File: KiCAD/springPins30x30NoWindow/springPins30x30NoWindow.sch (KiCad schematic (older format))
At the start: 21 parts, among them J1 CONN_02X06, J2 CONN_02X06

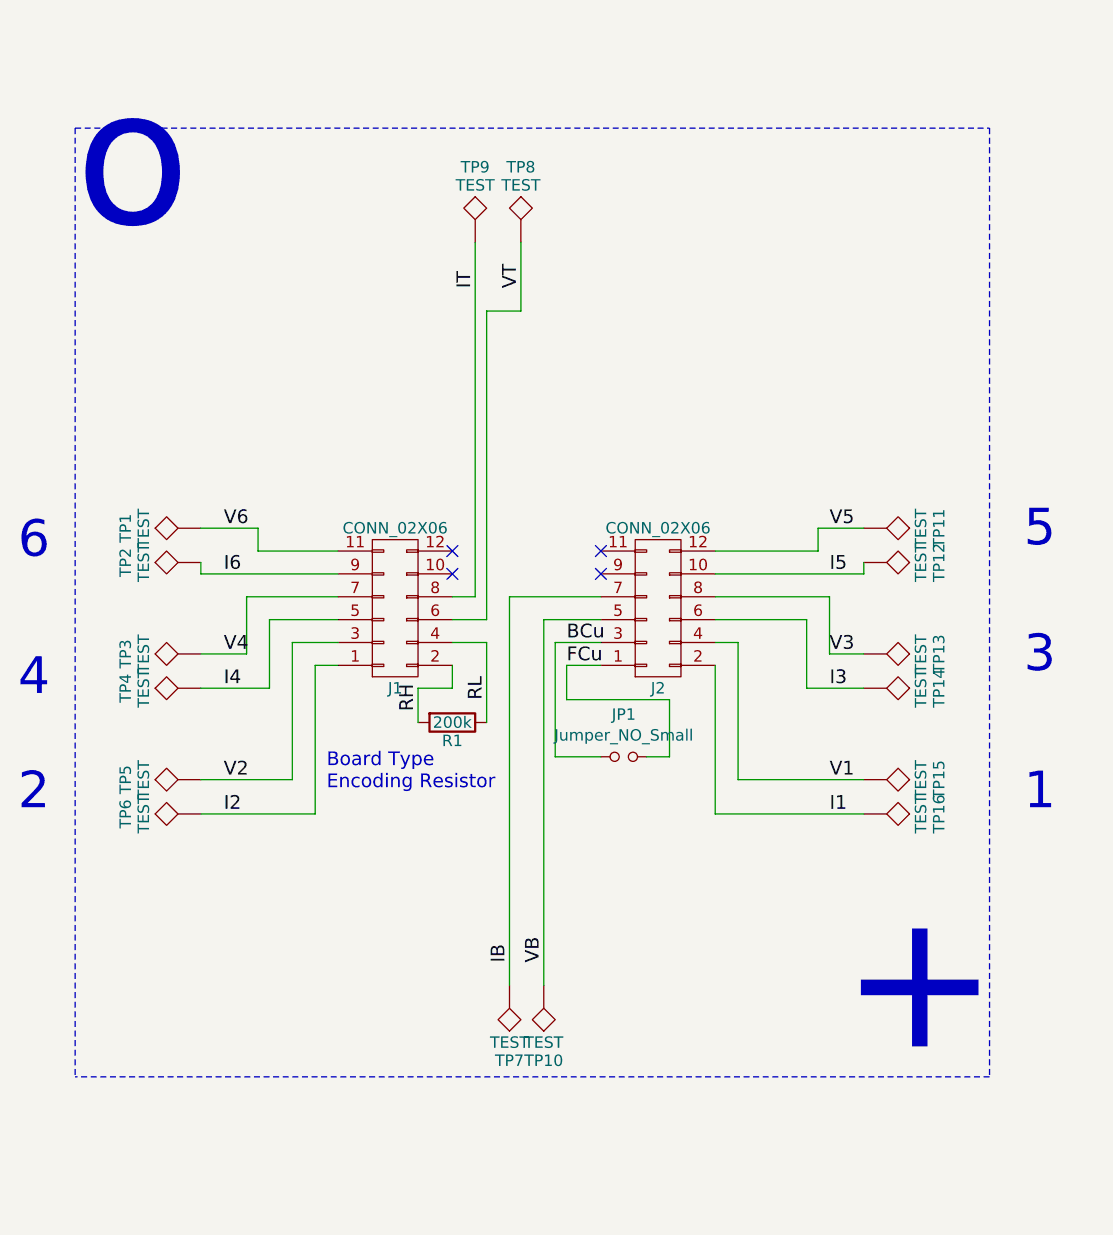
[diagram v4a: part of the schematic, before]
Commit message: go back to old 30x30 springpins layout
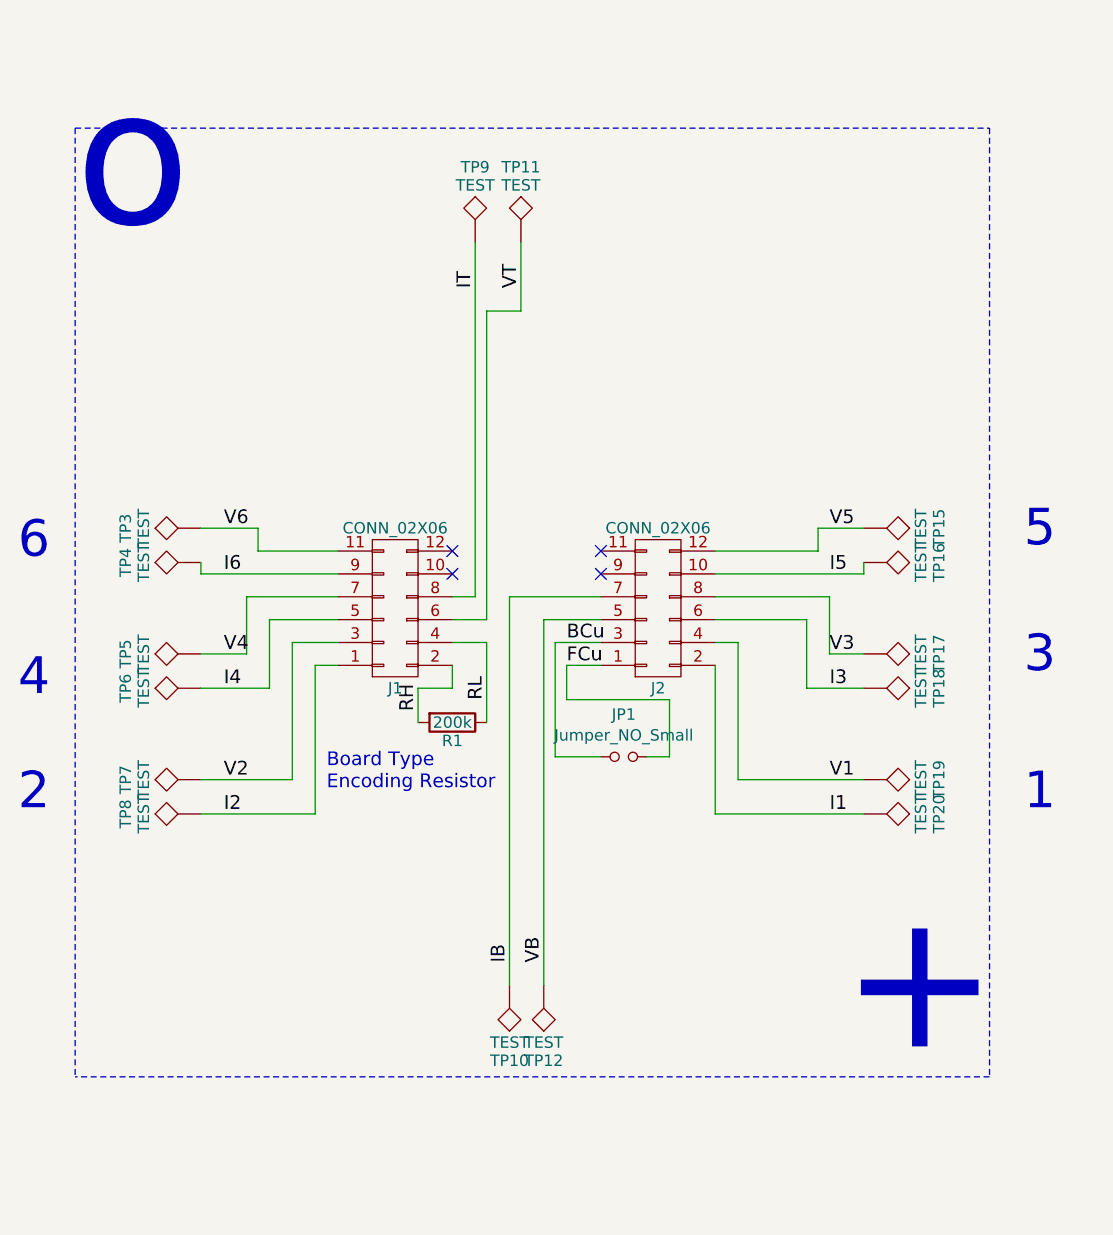
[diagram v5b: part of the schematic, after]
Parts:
- removed TP1, TP13, TP14, TP2: TEST, myParts:S25-022+P25-4023, symbol TEST
- added TP17, TP18, TP19, TP20: TEST, myParts:S25-022+P25-4023, symbol TEST
- TP10, TP11, TP12, TP15, TP16, TP3, TP4, TP5, TP6, TP7, TP8, TP9: farnellCode 9960260 + 9960244 -> (none)
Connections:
- net I1: now also TP20.1; no longer TP16.1
- net I2: now also TP8.1; no longer TP6.1
- net I3: now also TP18.1
- net I4: now also TP6.1; no longer TP4.1
- net I5: now also TP16.1; no longer TP12.1
- net I6: now also TP4.1
- net IB: now also TP10.1; no longer TP7.1
- net V1: now also TP19.1; no longer TP15.1
- net V2: now also TP7.1; no longer TP5.1
- net V3: now also TP17.1
- net V4: now also TP5.1; no longer TP3.1
- net V5: now also TP15.1; no longer TP11.1
- net V6: now also TP3.1
- net VB: now also TP12.1; no longer TP10.1
- net VT: now also TP11.1; no longer TP8.1
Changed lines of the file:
@@
 LIBS:power
 LIBS:device
+LIBS:transistors
+LIBS:conn
 LIBS:linear
 LIBS:regul
+LIBS:74xx
+LIBS:cmos4000
 LIBS:adc-dac
 LIBS:memory
@@
 LIBS:digital-audio
 LIBS:philips
+LIBS:display
 LIBS:cypress
 LIBS:siliconi
@@
 LIBS:atmel
 LIBS:contrib
+LIBS:valves
 LIBS:springPins30x30NoWindow-cache
 EELAYER 26 0
@@
 $EndDescr
 $Comp
+L TEST TP10
+U 1 1 58E4C4C8
+P 5100 5550
+F 0 "TP10" H 5100 5850 50  0000 C BNN
+F 1 "TEST" H 5100 5800 50  0000 C CNN
+F 2 "myParts:S25-022+P25-4023" H 5100 5550 50  0001 C CNN
+F 3 "" H 5100 5550 50  0000 C CNN
+	1    5100 5550
+	-1   0    0    1
+$EndComp
+$Comp
+L TEST TP6
+U 1 1 58E4C4F2
+P 3750 4250
+F 0 "TP6" H 3750 4550 50  0000 C BNN
+F 1 "TEST" H 3750 4500 50  0000 C CNN
+F 2 "myParts:S25-022+P25-4023" H 3750 4250 50  0001 C CNN
+F 3 "" H 3750 4250 50  0000 C CNN
+	1    3750 4250
+	0    -1   -1   0
+$EndComp
+$Comp
+L TEST TP5
+U 1 1 58E4C553
+P 3750 4100
+F 0 "TP5" H 3750 4400 50  0000 C BNN
+F 1 "TEST" H 3750 4350 50  0000 C CNN
+F 2 "myParts:S25-022+P25-4023" H 3750 4100 50  0001 C CNN
+F 3 "" H 3750 4100 50  0000 C CNN
+	1    3750 4100
+	0    -1   -1   0
+$EndComp
+$Comp
+L TEST TP8
+U 1 1 58E4C6B7
+P 3750 4800
+F 0 "TP8" H 3750 5100 50  0000 C BNN
+F 1 "TEST" H 3750 5050 50  0000 C CNN
+F 2 "myParts:S25-022+P25-4023" H 3750 4800 50  0001 C CNN
+F 3 "" H 3750 4800 50  0000 C CNN
+	1    3750 4800
+	0    -1   -1   0
+$EndComp
+$Comp
+L TEST TP7
+U 1 1 58E4C6BD
+P 3750 4650
+F 0 "TP7" H 3750 4950 50  0000 C BNN
+F 1 "TEST" H 3750 4900 50  0000 C CNN
+F 2 "myParts:S25-022+P25-4023" H 3750 4650 50  0001 C CNN
+F 3 "" H 3750 4650 50  0000 C CNN
+	1    3750 4650
+	0    -1   -1   0
+$EndComp
+$Comp
+L TEST TP4
+U 1 1 58E4C747
+P 3750 3700
+F 0 "TP4" H 3750 4000 50  0000 C BNN
+F 1 "TEST" H 3750 3950 50  0000 C CNN
+F 2 "myParts:S25-022+P25-4023" H 3750 3700 50  0001 C CNN
+F 3 "" H 3750 3700 50  0000 C CNN
+	1    3750 3700
+	0    -1   -1   0
+$EndComp
+$Comp
+L TEST TP3
+U 1 1 58E4C74D
+P 3750 3550
+F 0 "TP3" H 3750 3850 50  0000 C BNN
+F 1 "TEST" H 3750 3800 50  0000 C CNN
+F 2 "myParts:S25-022+P25-4023" H 3750 3550 50  0001 C CNN
+F 3 "" H 3750 3550 50  0000 C CNN
+	1    3750 3550
+	0    -1   -1   0
+$EndComp
+$Comp
+L TEST TP18
+U 1 1 58E4CA5F
+P 6650 4250
+F 0 "TP18" H 6650 4550 50  0000 C BNN
+F 1 "TEST" H 6650 4500 50  0000 C CNN
+F 2 "myParts:S25-022+P25-4023" H 6650 4250 50  0001 C CNN
+F 3 "" H 6650 4250 50  0000 C CNN
+	1    6650 4250
+	0    1    -1   0
+$EndComp
+$Comp
+L TEST TP17
+U 1 1 58E4CA65
+P 6650 4100
+F 0 "TP17" H 6650 4400 50  0000 C BNN
+F 1 "TEST" H 6650 4350 50  0000 C CNN
+F 2 "myParts:S25-022+P25-4023" H 6650 4100 50  0001 C CNN
+F 3 "" H 6650 4100 50  0000 C CNN
+	1    6650 4100
+	0    1    -1   0
+$EndComp
+$Comp
+L TEST TP20
+U 1 1 58E4CA6B
+P 6650 4800
+F 0 "TP20" H 6650 5100 50  0000 C BNN
+F 1 "TEST" H 6650 5050 50  0000 C CNN
+F 2 "myParts:S25-022+P25-4023" H 6650 4800 50  0001 C CNN
+F 3 "" H 6650 4800 50  0000 C CNN
+	1    6650 4800
+	0    1    -1   0
+$EndComp
+$Comp
+L TEST TP19
+U 1 1 58E4CA71
+P 6650 4650
+F 0 "TP19" H 6650 4950 50  0000 C BNN
+F 1 "TEST" H 6650 4900 50  0000 C CNN
+F 2 "myParts:S25-022+P25-4023" H 6650 4650 50  0001 C CNN
+F 3 "" H 6650 4650 50  0000 C CNN
+	1    6650 4650
+	0    1    -1   0
+$EndComp
+$Comp
+L TEST TP16
+U 1 1 58E4CA77
+P 6650 3700
+F 0 "TP16" H 6650 4000 50  0000 C BNN
+F 1 "TEST" H 6650 3950 50  0000 C CNN
+F 2 "myParts:S25-022+P25-4023" H 6650 3700 50  0001 C CNN
+F 3 "" H 6650 3700 50  0000 C CNN
+	1    6650 3700
+	0    1    -1   0
+$EndComp
+$Comp
+L TEST TP15
+U 1 1 58E4CA7D
+P 6650 3550
+F 0 "TP15" H 6650 3850 50  0000 C BNN
+F 1 "TEST" H 6650 3800 50  0000 C CNN
+F 2 "myParts:S25-022+P25-4023" H 6650 3550 50  0001 C CNN
+F 3 "" H 6650 3550 50  0000 C CNN
+	1    6650 3550
+	0    1    -1   0
+$EndComp
+$Comp
 L TEST TP9
 U 1 1 58E4CC43
@@
 F 2 "myParts:S25-022+P25-4023" H 4950 2300 50  0001 C CNN
 F 3 "" H 4950 2300 50  0000 C CNN
-F 4 "9960260 + 9960244" H 4950 2300 60  0001 C CNN "farnellCode"
 	1    4950 2300
+	-1   0    0    -1
+$EndComp
+$Comp
+L TEST TP11
+U 1 1 58E4CC49
+P 5150 2300
+F 0 "TP11" H 5150 2600 50  0000 C BNN
+F 1 "TEST" H 5150 2550 50  0000 C CNN
+F 2 "myParts:S25-022+P25-4023" H 5150 2300 50  0001 C CNN
+F 3 "" H 5150 2300 50  0000 C CNN
+	1    5150 2300
 	-1   0    0    -1
 $EndComp
@@
 Wire Wire Line
 	4000 3550 3750 3550
+$Comp
+L TEST TP12
+U 1 1 58E4C3ED
+P 5250 5550
+F 0 "TP12" H 5250 5850 50  0000 C BNN
+F 1 "TEST" H 5250 5800 50  0000 C CNN
+F 2 "myParts:S25-022+P25-4023" H 5250 5550 50  0001 C CNN
+F 3 "" H 5250 5550 50  0000 C CNN
+	1    5250 5550
+	-1   0    0    1
+$EndComp
 Wire Wire Line
 	4950 2300 4950 3850
@@
 Wire Wire Line
 	5800 4550 5700 4550
-$Comp
-L TEST TP8
-U 1 1 5A65C96D
-P 5150 2300
-F 0 "TP8" H 5150 2600 50  0000 C BNN
-F 1 "TEST" H 5150 2550 50  0000 C CNN
-F 2 "myParts:S25-022+P25-4023" H 5150 2300 50  0001 C CNN
-F 3 "" H 5150 2300 50  0000 C CNN
-F 4 "9960260 + 9960244" H 5150 2300 60  0001 C CNN "farnellCode"
-	1    5150 2300
-	-1   0    0    -1
-$EndComp
-$Comp
-L TEST TP11
-U 1 1 5A65C9A7
-P 6650 3550
-F 0 "TP11" H 6650 3850 50  0000 C BNN
-F 1 "TEST" H 6650 3800 50  0000 C CNN
-F 2 "myParts:S25-022+P25-4023" H 6650 3550 50  0001 C CNN
-F 3 "" H 6650 3550 50  0000 C CNN
-F 4 "9960260 + 9960244" H 6650 3550 60  0001 C CNN "farnellCode"
-	1    6650 3550
-	0    1    -1   0
-$EndComp
-$Comp
-L TEST TP12
-U 1 1 5A65CA0A
-P 6650 3700
-F 0 "TP12" H 6650 4000 50  0000 C BNN
-F 1 "TEST" H 6650 3950 50  0000 C CNN
-F 2 "myParts:S25-022+P25-4023" H 6650 3700 50  0001 C CNN
-F 3 "" H 6650 3700 50  0000 C CNN
-F 4 "9960260 + 9960244" H 6650 3700 60  0001 C CNN "farnellCode"
-	1    6650 3700
-	0    1    -1   0
-$EndComp
-$Comp
-L TEST TP13
-U 1 1 5A65CA32
-P 6650 4100
-F 0 "TP13" H 6650 4400 50  0000 C BNN
-F 1 "TEST" H 6650 4350 50  0000 C CNN
-F 2 "myParts:S25-022+P25-4023" H 6650 4100 50  0001 C CNN
-F 3 "" H 6650 4100 50  0000 C CNN
-F 4 "9960260 + 9960244" H 6650 4100 60  0001 C CNN "farnellCode"
-	1    6650 4100
-	0    1    -1   0
-$EndComp
-$Comp
-L TEST TP14
-U 1 1 5A65CA62
-P 6650 4250
-F 0 "TP14" H 6650 4550 50  0000 C BNN
-F 1 "TEST" H 6650 4500 50  0000 C CNN
-F 2 "myParts:S25-022+P25-4023" H 6650 4250 50  0001 C CNN
-F 3 "" H 6650 4250 50  0000 C CNN
-F 4 "9960260 + 9960244" H 6650 4250 60  0001 C CNN "farnellCode"
-	1    6650 4250
-	0    1    -1   0
-$EndComp
-$Comp
-L TEST TP15
-U 1 1 5A65CA8E
-P 6650 4650
-F 0 "TP15" H 6650 4950 50  0000 C BNN
-F 1 "TEST" H 6650 4900 50  0000 C CNN
-F 2 "myParts:S25-022+P25-4023" H 6650 4650 50  0001 C CNN
-F 3 "" H 6650 4650 50  0000 C CNN
-F 4 "9960260 + 9960244" H 6650 4650 60  0001 C CNN "farnellCode"
-	1    6650 4650
-	0    1    -1   0
-$EndComp
-$Comp
-L TEST TP16
-U 1 1 5A65CAC6
-P 6650 4800
-F 0 "TP16" H 6650 5100 50  0000 C BNN
-F 1 "TEST" H 6650 5050 50  0000 C CNN
-F 2 "myParts:S25-022+P25-4023" H 6650 4800 50  0001 C CNN
-F 3 "" H 6650 4800 50  0000 C CNN
-F 4 "9960260 + 9960244" H 6650 4800 60  0001 C CNN "farnellCode"
-	1    6650 4800
-	0    1    -1   0
-$EndComp
-$Comp
-L TEST TP10
-U 1 1 5A65CAF2
-P 5250 5550
-F 0 "TP10" H 5250 5850 50  0000 C BNN
-F 1 "TEST" H 5250 5800 50  0000 C CNN
-F 2 "myParts:S25-022+P25-4023" H 5250 5550 50  0001 C CNN
-F 3 "" H 5250 5550 50  0000 C CNN
-F 4 "9960260 + 9960244" H 5250 5550 60  0001 C CNN "farnellCode"
-	1    5250 5550
-	1    0    0    1
-$EndComp
-$Comp
-L TEST TP7
-U 1 1 5A65CB55
-P 5100 5550
-F 0 "TP7" H 5100 5850 50  0000 C BNN
-F 1 "TEST" H 5100 5800 50  0000 C CNN
-F 2 "myParts:S25-022+P25-4023" H 5100 5550 50  0001 C CNN
-F 3 "" H 5100 5550 50  0000 C CNN
-F 4 "9960260 + 9960244" H 5100 5550 60  0001 C CNN "farnellCode"
-	1    5100 5550
-	1    0    0    1
-$EndComp
-$Comp
-L TEST TP6
-U 1 1 5A65CC03
-P 3750 4800
-F 0 "TP6" H 3750 5100 50  0000 C BNN
-F 1 "TEST" H 3750 5050 50  0000 C CNN
-F 2 "myParts:S25-022+P25-4023" H 3750 4800 50  0001 C CNN
-F 3 "" H 3750 4800 50  0000 C CNN
-F 4 "9960260 + 9960244" H 3750 4800 60  0001 C CNN "farnellCode"
-	1    3750 4800
-	0    -1   1    0
-$EndComp
-$Comp
-L TEST TP5
-U 1 1 5A65CC8C
-P 3750 4650
-F 0 "TP5" H 3750 4950 50  0000 C BNN
-F 1 "TEST" H 3750 4900 50  0000 C CNN
-F 2 "myParts:S25-022+P25-4023" H 3750 4650 50  0001 C CNN
-F 3 "" H 3750 4650 50  0000 C CNN
-F 4 "9960260 + 9960244" H 3750 4650 60  0001 C CNN "farnellCode"
-	1    3750 4650
-	0    -1   1    0
-$EndComp
-$Comp
-L TEST TP4
-U 1 1 5A65CCC0
-P 3750 4250
-F 0 "TP4" H 3750 4550 50  0000 C BNN
-F 1 "TEST" H 3750 4500 50  0000 C CNN
-F 2 "myParts:S25-022+P25-4023" H 3750 4250 50  0001 C CNN
-F 3 "" H 3750 4250 50  0000 C CNN
-F 4 "9960260 + 9960244" H 3750 4250 60  0001 C CNN "farnellCode"
-	1    3750 4250
-	0    -1   1    0
-$EndComp
-$Comp
-L TEST TP3
-U 1 1 5A65CCFE
-P 3750 4100
-F 0 "TP3" H 3750 4400 50  0000 C BNN
-F 1 "TEST" H 3750 4350 50  0000 C CNN
-F 2 "myParts:S25-022+P25-4023" H 3750 4100 50  0001 C CNN
-F 3 "" H 3750 4100 50  0000 C CNN
-F 4 "9960260 + 9960244" H 3750 4100 60  0001 C CNN "farnellCode"
-	1    3750 4100
-	0    -1   1    0
-$EndComp
-$Comp
-L TEST TP2
-U 1 1 5A65CD36
-P 3750 3700
-F 0 "TP2" H 3750 4000 50  0000 C BNN
-F 1 "TEST" H 3750 3950 50  0000 C CNN
-F 2 "myParts:S25-022+P25-4023" H 3750 3700 50  0001 C CNN
-F 3 "" H 3750 3700 50  0000 C CNN
-F 4 "9960260 + 9960244" H 3750 3700 60  0001 C CNN "farnellCode"
-	1    3750 3700
-	0    -1   1    0
-$EndComp
-$Comp
-L TEST TP1
-U 1 1 5A65CD7A
-P 3750 3550
-F 0 "TP1" H 3750 3850 50  0000 C BNN
-F 1 "TEST" H 3750 3800 50  0000 C CNN
-F 2 "myParts:S25-022+P25-4023" H 3750 3550 50  0001 C CNN
-F 3 "" H 3750 3550 50  0000 C CNN
-F 4 "9960260 + 9960244" H 3750 3550 60  0001 C CNN "farnellCode"
-	1    3750 3550
-	0    -1   1    0
-$EndComp
 $EndSCHEMATC

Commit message: spruce up spring pin boards
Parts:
- J1, J2: symbol CONN_02X06 -> Connector:Conn_02x06_Odd_Even
- JP1: symbol Jumper_NO_Small -> device:Jumper_NO_Small
- L1: symbol GREY@CHRISTOFORO.NET -> myParts:GREY@CHRISTOFORO.NET
- R1: symbol R -> device:R
- TP10, TP11, TP12, TP15, TP16, TP17, TP18, TP19, TP20, TP3, TP4, TP5, TP6, TP7, TP8, TP9: symbol TEST -> Connector:Test_Point
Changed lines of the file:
@@
-EESchema Schematic File Version 2
-LIBS:myParts
-LIBS:power
-LIBS:device
-LIBS:transistors
-LIBS:conn
-LIBS:linear
-LIBS:regul
-LIBS:74xx
-LIBS:cmos4000
-LIBS:adc-dac
-LIBS:memory
-LIBS:xilinx
-LIBS:microcontrollers
-LIBS:dsp
-LIBS:microchip
-LIBS:analog_switches
-LIBS:motorola
-LIBS:texas
-LIBS:intel
-LIBS:audio
-LIBS:interface
-LIBS:digital-audio
-LIBS:philips
-LIBS:display
-LIBS:cypress
-LIBS:siliconi
-LIBS:opto
-LIBS:atmel
-LIBS:contrib
-LIBS:valves
+EESchema Schematic File Version 4
 LIBS:springPins30x30NoWindow-cache
 EELAYER 26 0
@@
 $EndDescr
 $Comp
-L TEST TP10
+L Connector:Test_Point TP10
 U 1 1 58E4C4C8
 P 5100 5550
@@
 $EndComp
 $Comp
-L TEST TP6
+L Connector:Test_Point TP6
 U 1 1 58E4C4F2
 P 3750 4250
@@
 $EndComp
 $Comp
-L TEST TP5
+L Connector:Test_Point TP5
 U 1 1 58E4C553
 P 3750 4100
@@
 $EndComp
 $Comp
-L TEST TP8
+L Connector:Test_Point TP8
 U 1 1 58E4C6B7
 P 3750 4800
@@
 $EndComp
 $Comp
-L TEST TP7
+L Connector:Test_Point TP7
 U 1 1 58E4C6BD
 P 3750 4650
@@
 $EndComp
 $Comp
-L TEST TP4
+L Connector:Test_Point TP4
 U 1 1 58E4C747
 P 3750 3700
@@
 $EndComp
 $Comp
-L TEST TP3
+L Connector:Test_Point TP3
 U 1 1 58E4C74D
 P 3750 3550
@@
 $EndComp
 $Comp
-L TEST TP18
+L Connector:Test_Point TP18
 U 1 1 58E4CA5F
 P 6650 4250
@@
 $EndComp
 $Comp
-L TEST TP17
+L Connector:Test_Point TP17
 U 1 1 58E4CA65
 P 6650 4100
@@
 $EndComp
 $Comp
-L TEST TP20
+L Connector:Test_Point TP20
 U 1 1 58E4CA6B
 P 6650 4800
@@
 $EndComp
 $Comp
-L TEST TP19
+L Connector:Test_Point TP19
 U 1 1 58E4CA71
 P 6650 4650
@@
 $EndComp
 $Comp
-L TEST TP16
+L Connector:Test_Point TP16
 U 1 1 58E4CA77
 P 6650 3700
@@
 $EndComp
 $Comp
-L TEST TP15
+L Connector:Test_Point TP15
 U 1 1 58E4CA7D
 P 6650 3550
@@
 $EndComp
 $Comp
-L TEST TP9
+L Connector:Test_Point TP9
 U 1 1 58E4CC43
 P 4950 2300
@@
 $EndComp
 $Comp
-L TEST TP11
+L Connector:Test_Point TP11
 U 1 1 58E4CC49
 P 5150 2300
@@
 6
 $Comp
-L CONN_02X06 J1
+L Connector:Conn_02x06_Odd_Even J1
 U 1 1 599DB107
-P 4600 3900
-F 0 "J1" H 4600 4250 50  0000 C CNN
-F 1 "CONN_02X06" H 4600 3550 50  0000 C CNN
-F 2 "Pin_Headers:Pin_Header_Straight_2x06_Pitch2.54mm" H 4600 2700 50  0001 C CNN
-F 3 "" H 4600 2700 50  0001 C CNN
-	1    4600 3900
+P 4550 3950
+F 0 "J1" H 4450 4250 50  0000 C CNN
+F 1 "CONN_02X06" H 4550 3500 50  0000 C CNN
+F 2 "Pin_Headers:Pin_Header_Straight_2x06_Pitch2.54mm" H 4550 2750 50  0001 C CNN
+F 3 "" H 4550 2750 50  0001 C CNN
+	1    4550 3950
 	1    0    0    1
 $EndComp
 $Comp
-L CONN_02X06 J2
+L Connector:Conn_02x06_Odd_Even J2
 U 1 1 599DB1BB
-P 5750 3900
-F 0 "J2" H 5750 4250 50  0000 C CNN
-F 1 "CONN_02X06" H 5750 3550 50  0000 C CNN
-F 2 "Pin_Headers:Pin_Header_Straight_2x06_Pitch2.54mm" H 5750 2700 50  0001 C CNN
-F 3 "" H 5750 2700 50  0001 C CNN
-	1    5750 3900
+P 5700 3950
+F 0 "J2" H 5600 4250 50  0000 C CNN
+F 1 "CONN_02X06" H 5700 3500 50  0000 C CNN
+F 2 "Pin_Headers:Pin_Header_Straight_2x06_Pitch2.54mm" H 5700 2750 50  0001 C CNN
+F 3 "" H 5700 2750 50  0001 C CNN
+	1    5700 3950
 	1    0    0    1
 $EndComp
 $Comp
-L R R1
+L device:R R1
 U 1 1 599DBDE1
 P 4850 4400
@@
 	4000 3550 3750 3550
 $Comp
-L TEST TP12
+L Connector:Test_Point TP12
 U 1 1 58E4C3ED
 P 5250 5550
@@
 NoConn ~ 4850 3750
 $Comp
-L GREY@CHRISTOFORO.NET L1
+L myParts:GREY@CHRISTOFORO.NET L1
 U 1 1 59BFB10C
 P 7950 6950
@@
 $EndComp
 $Comp
-L Jumper_NO_Small JP1
+L device:Jumper_NO_Small JP1
 U 1 1 59F4B423
 P 5600 4550
